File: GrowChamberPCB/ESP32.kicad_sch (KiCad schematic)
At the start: 29 parts, among them SW1 Reset_Button_Internal, SW3 Bootmode_Internal, U3 ESP32-S3-WROOM-1U-N8R8, U7 TC4428EOA, U8 W25Q128JVSIQTR

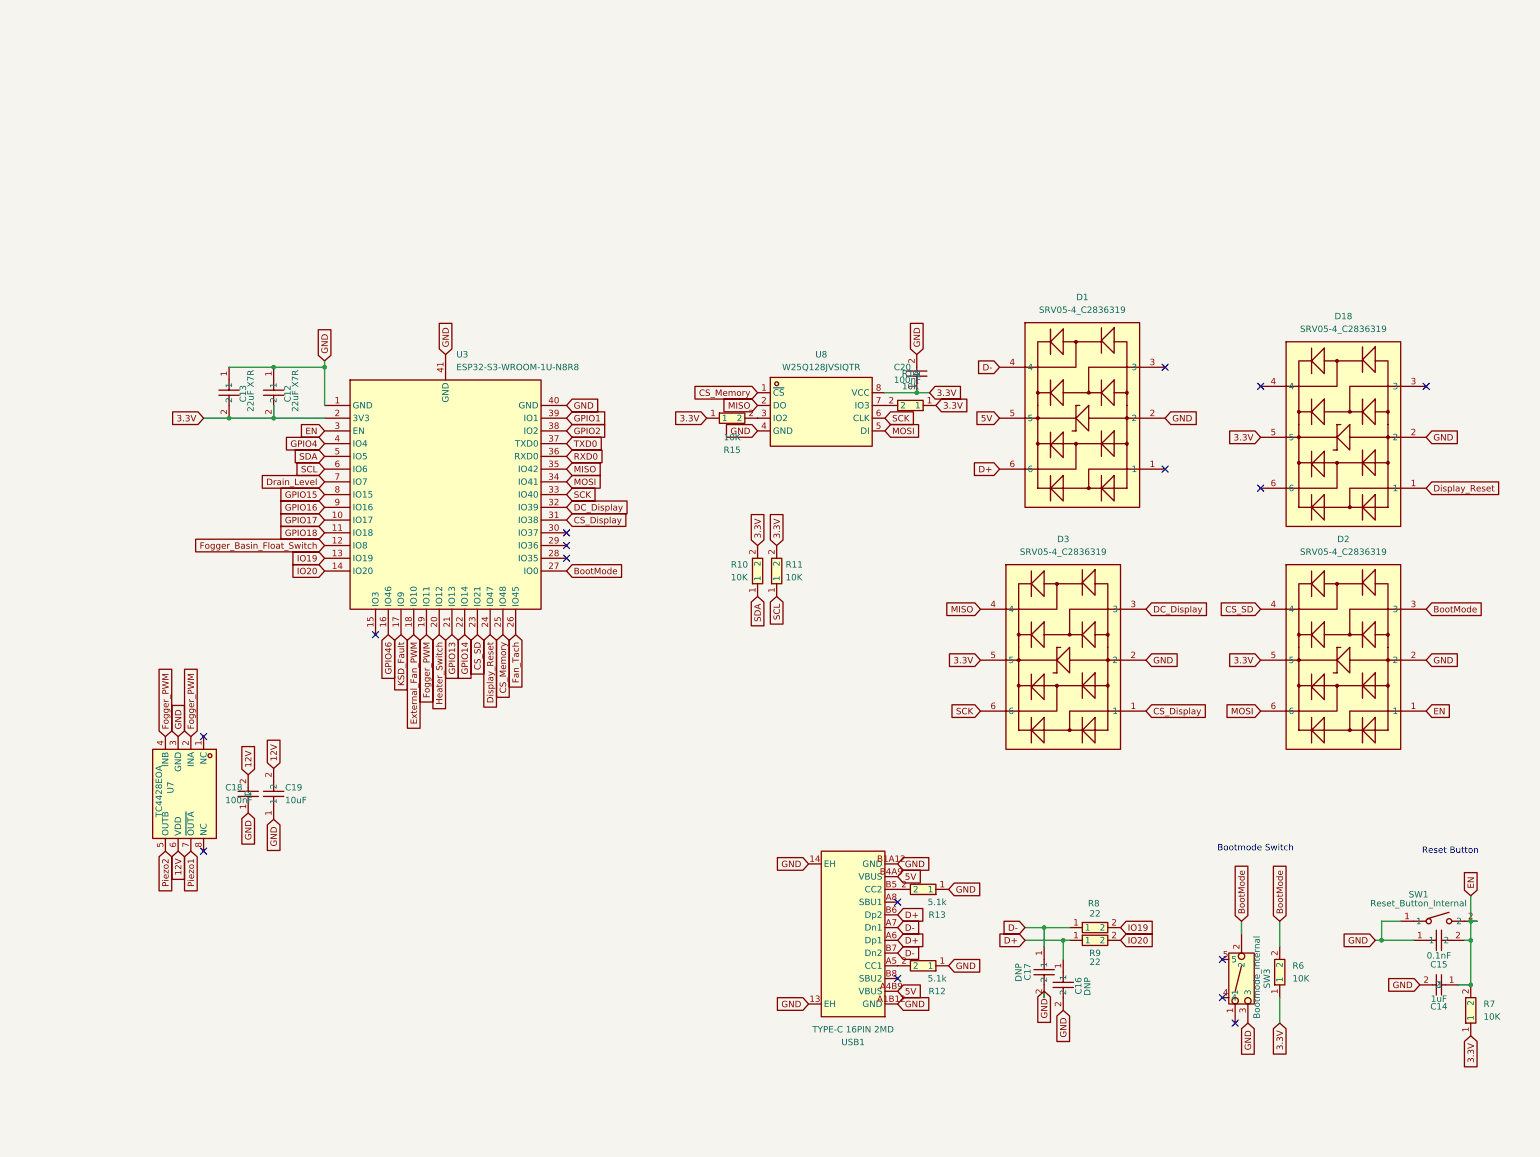
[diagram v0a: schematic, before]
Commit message: Removed 3.3V, wired some stuff
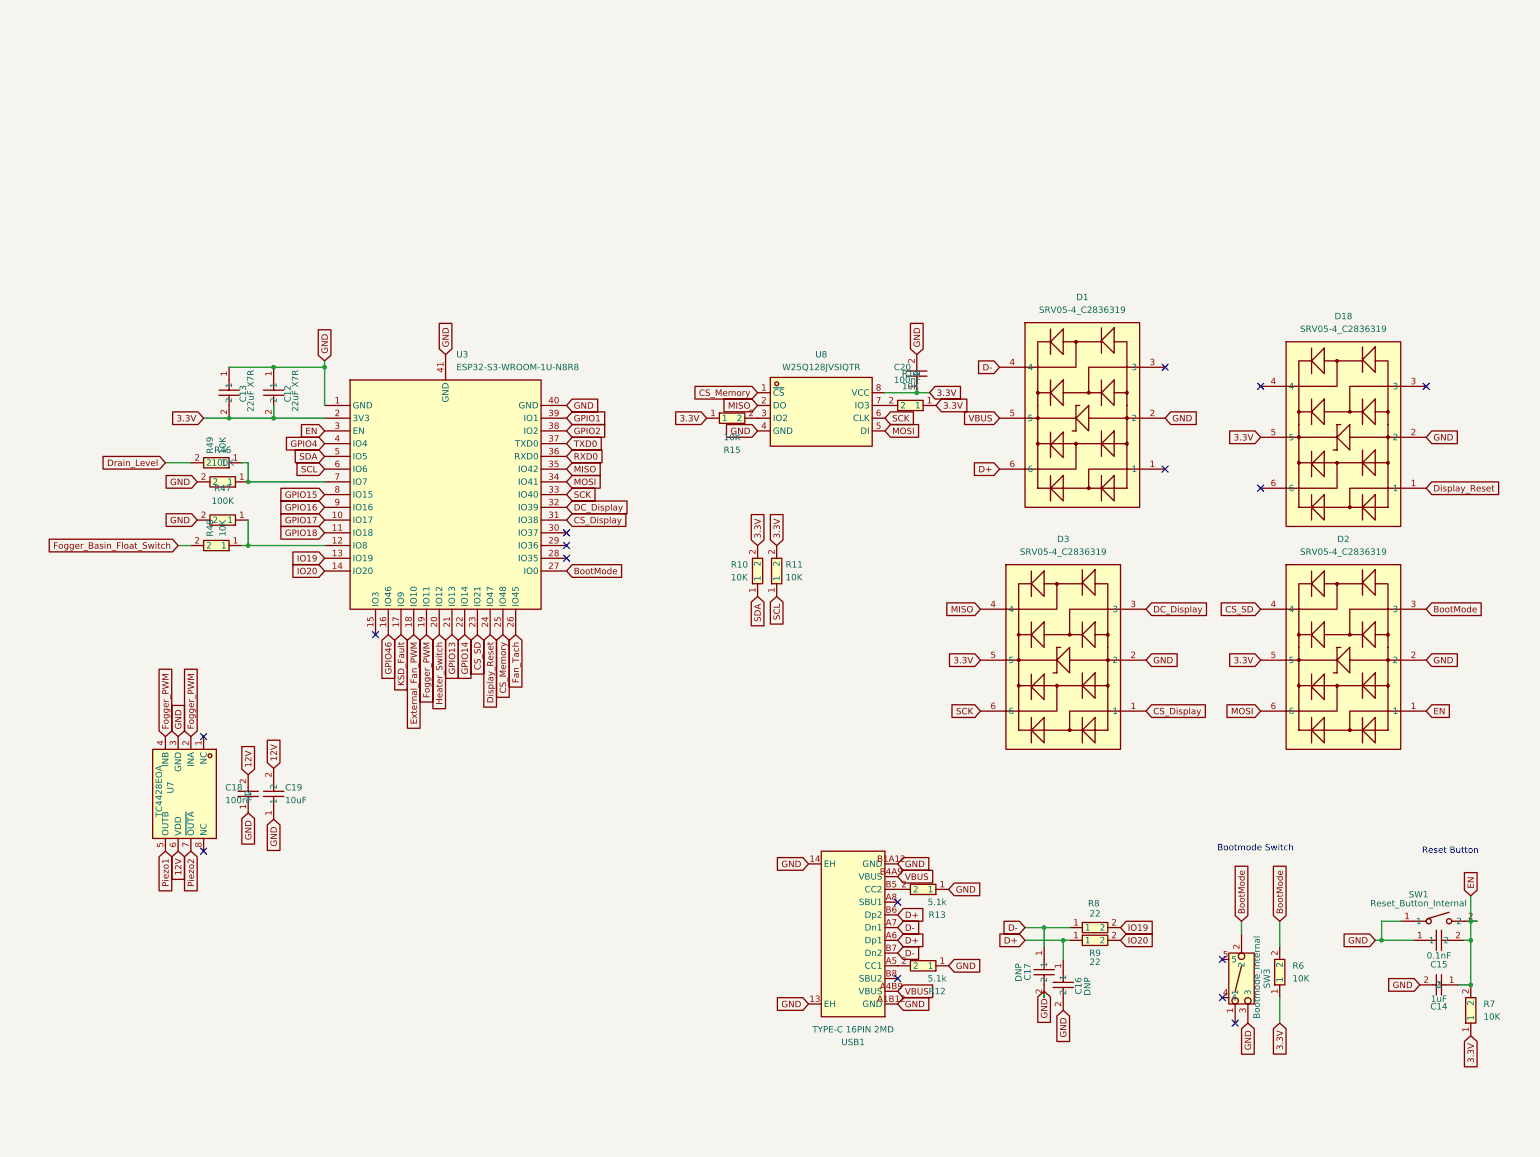
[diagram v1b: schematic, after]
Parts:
- added R46, R47: 100K, easyeda2kicad:R0603, symbol easyeda2kicad:RT0603BRD07100KL
- added R48, R49: 10K, easyeda2kicad:R0603, symbol easyeda2kicad:AC0603FR-0710KL
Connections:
- net Drain_Level: now also R49.2; no longer U3.7 (IO7)
- net Fogger_Basin_Float_Switch: now also R48.2; no longer U3.12 (IO8)
- net GND: now also R46.2, R47.2
- net Piezo1: now also U7.5 (OUTB); no longer U7.7 (~{OUTA})
- net Piezo2: now also U7.7 (~{OUTA}); no longer U7.5 (OUTB)
- net 5V renamed VBUS
- new net: R46.1, R49.1, U3.7 (IO7)
- new net: R47.1, R48.1, U3.12 (IO8)

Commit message: failing to route the board
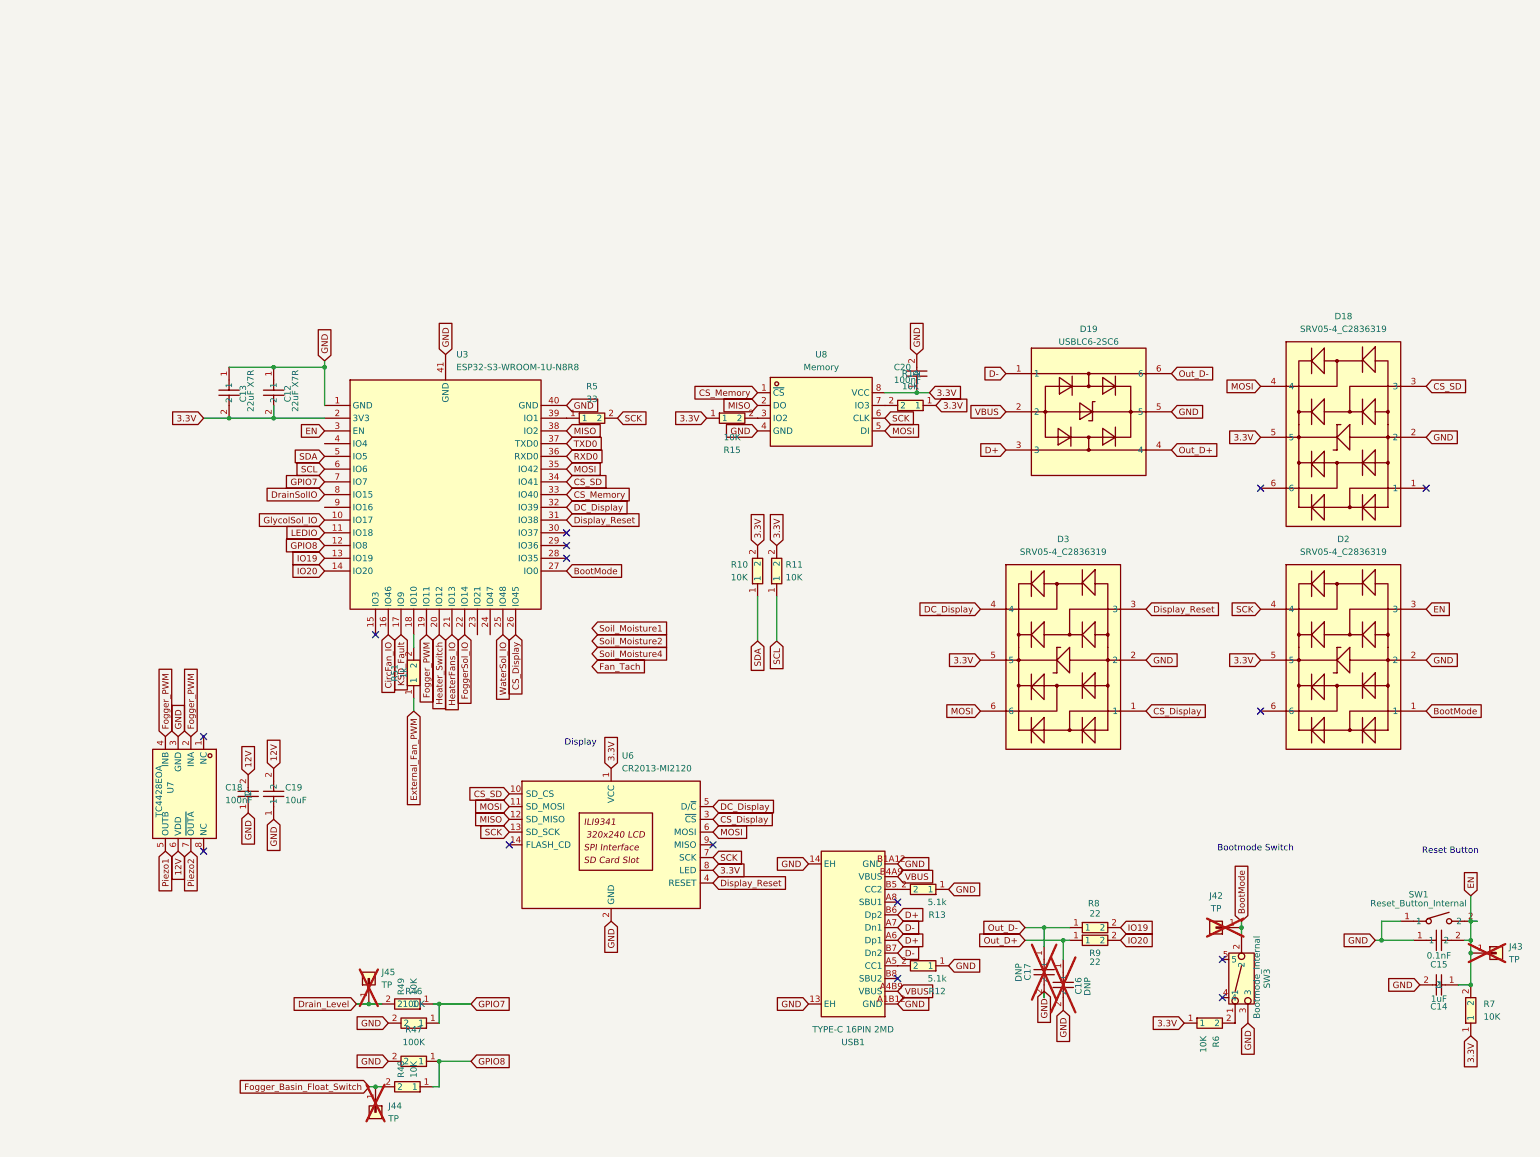
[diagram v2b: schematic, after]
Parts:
- removed D1: SRV05-4_C2836319, easyeda2kicad:SOT-23-6_L2.9-W1.6-P0.95-LS2.8-BL, symbol easyeda2kicad:SRV05-4_C2836319
- added D19: USBLC6-2SC6, easyeda2kicad:SOT-23-6_L2.9-W1.6-P0.95-LS2.8-BL, symbol easyeda2kicad:USBLC6-2SC6
- added J42, J43, J44, J45: TP, TestPoint:TestPoint_Pad_D2.0mm, symbol Connector_Generic:Conn_01x01
- added R5: 33, easyeda2kicad:R0603, symbol easyeda2kicad:RS-03K33R0FT
- added R51: 1k, easyeda2kicad:R0603, symbol easyeda2kicad:FRC0603J102TS
- added U6: CR2013-MI2120, Connector_PinHeader_2.54mm:PinHeader_1x14_P2.54mm_Vertical, symbol Driver_Display:CR2013-MI2120
- C16, C17: now not fitted; now left out of the parts list
- U8: value W25Q128JVSIQTR -> Memory
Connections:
- net GPIO2 is gone; now on net MISO: U3.38 (IO2)
- net 3.3V: now also U6.1 (VCC), U6.8 (LED)
- net BootMode: now also D2.1, J42.1 (Pin_1); no longer D2.3, R6.2
- net CS_Display: now also U3.26 (IO45), U6.3 (~{CS}); no longer U3.31 (IO38)
- net CS_Memory: now also U3.33 (IO40); no longer U3.25 (IO48)
- net CS_SD: now also D18.3, U3.34 (IO41), U6.10 (SD_CS); no longer D2.4, U3.23 (IO21)
- net D+: now also D19.3; no longer C16.1, R9.1
- net D-: now also D19.1; no longer C17.1, R8.1
- net DC_Display: now also D3.4, U6.5 (D/~{C}); no longer D3.3
- net Display_Reset: now also D3.3, U3.31 (IO38), U6.4 (RESET); no longer D18.1, U3.24 (IO47)
- net Drain_Level: now also J45.1 (Pin_1)
- net EN: now also D2.3, J43.1 (Pin_1); no longer D2.1
- net External_Fan_PWM: now also R51.1; no longer U3.18 (IO10)
- net Fan_Tach: no longer U3.26 (IO45)
- net Fogger_Basin_Float_Switch: now also J44.1 (Pin_1)
- net GND: now also D19.5, U6.2 (GND)
- net MISO: now also U6.12 (SD_MISO); no longer D3.4, U3.35 (IO42)
- net MOSI: now also D18.4, D3.6, U3.35 (IO42), U6.11 (SD_MOSI), U6.6 (MOSI); no longer D2.6, U3.34 (IO41)
- net SCK: now also D2.4, R5.2, U6.13 (SD_SCK), U6.7 (SCK); no longer D3.6, U3.33 (IO40)
- net VBUS: now also D19.2
- net GPIO7: now reaches R46.1, R49.1, U3.7 (IO7)
- net GPIO8: now reaches R47.1, R48.1, U3.12 (IO8)
- net at SW3.1: now also R6.2
- net GPIO1: no longer names the net of U3.39 (IO1)
- net GPIO1: now also R5.1
- net GPIO13 renamed HeaterFans_IO
- net GPIO14 renamed FoggerSol_IO
- net GPIO15 renamed DrainSolIO
- net GPIO16: no longer names the net of U3.9 (IO16)
- net GPIO17 renamed GlycolSol_IO
- net GPIO18 renamed LEDIO
- net GPIO4: no longer names the net of U3.4 (IO4)
- net GPIO46 renamed CircFan_IO
- new net: R51.2, U3.18 (IO10)
- new net Out_D+: C16.1, D19.4, R9.1
- new net Out_D-: C17.1, D19.6, R8.1
- new net WaterSol_IO: U3.25 (IO48)
- no-connect marks 16 -> 15
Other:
- note added: "Display"
- moved on the sheet: R46, R47, R48, R49, R6

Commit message: almost done routing
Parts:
- removed D2: SRV05-4_C2836319, easyeda2kicad:SOT-23-6_L2.9-W1.6-P0.95-LS2.8-BL, symbol easyeda2kicad:SRV05-4_C2836319
- added D1: SRV05-4_C2836319, easyeda2kicad:SOT-23-6_L2.9-W1.6-P0.95-LS2.8-BL, symbol easyeda2kicad:SRV05-4_C2836319
- added R43, R54, R55, R56, R57: 33, easyeda2kicad:R0603, symbol easyeda2kicad:RS-03K33R0FT
- added U4: ZX-IDC2.54-2-13PZZ, easyeda2kicad:IDC-TH_26P-P2.54_ZX-IDC2.54-2-13PZZ, symbol easyeda2kicad:ZX-IDC2.54-2-13PZZ
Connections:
- net 3.3V: now also D1.5, U4.19
- net BootMode: now also D1.6
- net CS_Display: now also D3.3, R57.2; no longer D3.1, U3.26 (IO45)
- net CS_Memory: now also R56.2; no longer U3.33 (IO40)
- net CS_SD: now also D18.1, R55.2; no longer D18.3, U3.34 (IO41)
- net CircFan_IO: now also U3.18 (IO10); no longer U3.16 (IO46)
- net DC_Display: now also D3.6, U3.8 (IO15); no longer D3.4, U3.32 (IO39)
- net Display_Reset: now also D3.1, U3.6 (IO6); no longer D3.3, U3.31 (IO38)
- net DrainSolIO: now also U3.4 (IO4); no longer U3.8 (IO15)
- net Drain_Level: now also U4.16
- net EN: now also D1.1
- net External_Fan_PWM: now also U4.24
- net Fan_Tach: now also U3.39 (IO1), U4.26
- net FoggerSol_IO: now also U3.19 (IO11); no longer U3.22 (IO14)
- net Fogger_Basin_Float_Switch: now also U4.18
- net Fogger_PWM: now also U3.23 (IO21); no longer U3.19 (IO11)
- net GND: now also D1.2
- net GlycolSol_IO: now also U3.17 (IO9); no longer U3.10 (IO17)
- net HeaterFans_IO: now also U3.20 (IO12); no longer U3.21 (IO13)
- net Heater_Switch: now also U3.22 (IO14); no longer U3.20 (IO12)
- net KSD_Fault: now also U3.24 (IO47); no longer U3.17 (IO9)
- net LEDIO: now also U3.21 (IO13); no longer U3.11 (IO18)
- net MISO: now also D18.4, R43.2; no longer U3.38 (IO2)
- net MOSI: now also D18.6, D3.4, R54.2; no longer D18.4, D3.6, U3.35 (IO42)
- net Piezo1: now also U4.3
- net Piezo2: now also U4.1
- net RXD0: now also U4.20
- net SCK: now also D18.3
- net SCL: now also U3.26 (IO45), U4.25; no longer U3.6 (IO6)
- net SDA: now also U3.25 (IO48), U4.23; no longer U3.5 (IO5)
- net Soil_Moisture1: now also U3.33 (IO40), U4.14
- net Soil_Moisture2: now also U3.32 (IO39), U4.12
- net Soil_Moisture4: now also U3.31 (IO38), U4.10
- net TXD0: now also U4.22
- net WaterSol_IO: now also U3.16 (IO46); no longer U3.25 (IO48)
- net at R5.1: now also U3.12 (IO8); no longer U3.39 (IO1)
- net at R51.2: now also U3.38 (IO2); no longer U3.18 (IO10)
- net at U3.9 (IO16): now also R54.1
- net GPIO7 renamed DrainLevel_IO
- net DrainLevel_IO: now also U3.34 (IO41); no longer U3.7 (IO7)
- net GPIO8 renamed FloatSwitch_IO
- net FloatSwitch_IO: now also U3.35 (IO42); no longer U3.12 (IO8)
- new net: R43.1, U3.10 (IO17)
- new net: R55.1, U3.7 (IO7)
- new net: R56.1, U3.11 (IO18)
- new net: R57.1, U3.5 (IO5)
- no-connect marks 15 -> 14
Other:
- moved on the sheet: R5, R51

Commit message: working on pcb
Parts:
- removed R14: 10K, easyeda2kicad:R0603, symbol easyeda2kicad:AC0603FR-0710KL
- removed U6: CR2013-MI2120, Connector_PinHeader_2.54mm:PinHeader_1x14_P2.54mm_Vertical, symbol Driver_Display:CR2013-MI2120
- added J47: Conn_01x04, Connector_PinSocket_2.54mm:PinSocket_1x04_P2.54mm_Vertical, symbol Connector_Generic:Conn_01x04
- added J48: Conn_01x09, Connector_PinSocket_2.54mm:PinSocket_1x09_P2.54mm_Vertical, symbol Connector_Generic:Conn_01x09
- added LED13: 12V On, easyeda2kicad:LED-TH_BD3.9-P2.54-RD_RED, symbol easyeda2kicad:EL304RD
- added R50: 10K, easyeda2kicad:R0603, symbol easyeda2kicad:AC0603FR-0710KL
- added R58, R59: 33, easyeda2kicad:R0603, symbol easyeda2kicad:RS-03K33R0FT
- added R60: 1k, easyeda2kicad:R0603, symbol easyeda2kicad:FRC0603J102TS
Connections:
- net 12V: now also R60.2
- net 3.3V: now also U4.2, U4.4, J48.1 (Pin_1), J48.8 (Pin_8), R50.1; no longer U4.19
- net BootMode: now also U4.8
- net CS_Display: now also J48.3 (Pin_3)
- net CS_Memory: now also R54.2; no longer R56.2
- net CS_SD: now also D18.6, J47.1 (Pin_1); no longer D18.1
- net Circ_Fan: now also U4.19
- net DC_Display: now also U3.7 (IO7), J48.5 (Pin_5); no longer U3.8 (IO15)
- net Display_Reset: now also J48.4 (Pin_4)
- net DrainSol: now also U4.17
- net EN: now also U4.6
- net FoggerSol: now also U4.13
- net GND: now also J48.2 (Pin_2)
- net GlycolSol: now also U4.11
- net Heater Fans: now also U4.15
- net Heater_ON: now also U4.5
- net LEDs: now also U4.7
- net MISO: now also J47.3 (Pin_3)
- net MOSI: now also D18.1, R56.2, J47.2 (Pin_2), J48.6 (Pin_6); no longer D18.6, D3.4, R54.2
- net RXD0: now also R58.1; no longer U3.36 (RXD0)
- net SCK: now also J47.4 (Pin_4), J48.7 (Pin_7)
- net TXD0: now also R59.1; no longer U3.37 (TXD0)
- net WaterSol: now also U4.9
- net at R43.1: now also U3.9 (IO16); no longer U3.10 (IO17)
- net at R55.1: now also U3.12 (IO8); no longer U3.7 (IO7)
- net at R5.1: now also U3.11 (IO18); no longer U3.12 (IO8)
- net at R54.1: now also U3.8 (IO15); no longer U3.9 (IO16)
- net at U8.7 (IO3): now also R50.2
- net at R56.1: now also U3.10 (IO17); no longer U3.11 (IO18)
- new net: LED13.2 (A), R60.1
- new net: R59.2, U3.37 (TXD0)
- new net: R58.2, U3.36 (RXD0)
- new net GND_FP: LED13.1 (K)
- no-connect marks 14 -> 13
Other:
- note removed: "Display"
- moved on the sheet: D1

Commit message: made a 4 layer board instead of 2
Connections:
- net GND_FP is gone; now on net GND: LED13.1 (K)
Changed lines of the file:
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@@
 		)
 	)
-	(global_label "GND_FP"
+	(global_label "GND"
 		(shape input)
 		(at 111.76 177.8 180)
@@
 		)
 		(property "Intersheetrefs" "${INTERSHEET_REFS}"
-			(at 101.5781 177.8 0)
+			(at 104.9043 177.8 0)
 			(hide yes)
 			(show_name no)

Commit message: fillin stuff out
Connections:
- no-connect marks 13 -> 14
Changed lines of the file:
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@@
+	)
+	(no_connect
+		(at 58.42 -5.08)
 	)
 	(no_connect

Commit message: redesign 3
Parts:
- removed U4: ZX-IDC2.54-2-13PZZ, easyeda2kicad:IDC-TH_26P-P2.54_ZX-IDC2.54-2-13PZZ, symbol easyeda2kicad:ZX-IDC2.54-2-13PZZ
- J47, J48: now not fitted; now left out of the parts list
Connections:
- no-connect marks 14 -> 13
